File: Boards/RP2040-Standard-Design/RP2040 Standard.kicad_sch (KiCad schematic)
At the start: 38 parts, among them J2 BM03B-SRSS-TBLFSN, J4 DX07S016JA1R1500, U1 ST1L05APU33R, U2 W25Q128JVSIQ TR, U3 ESD7L5.0DT5G

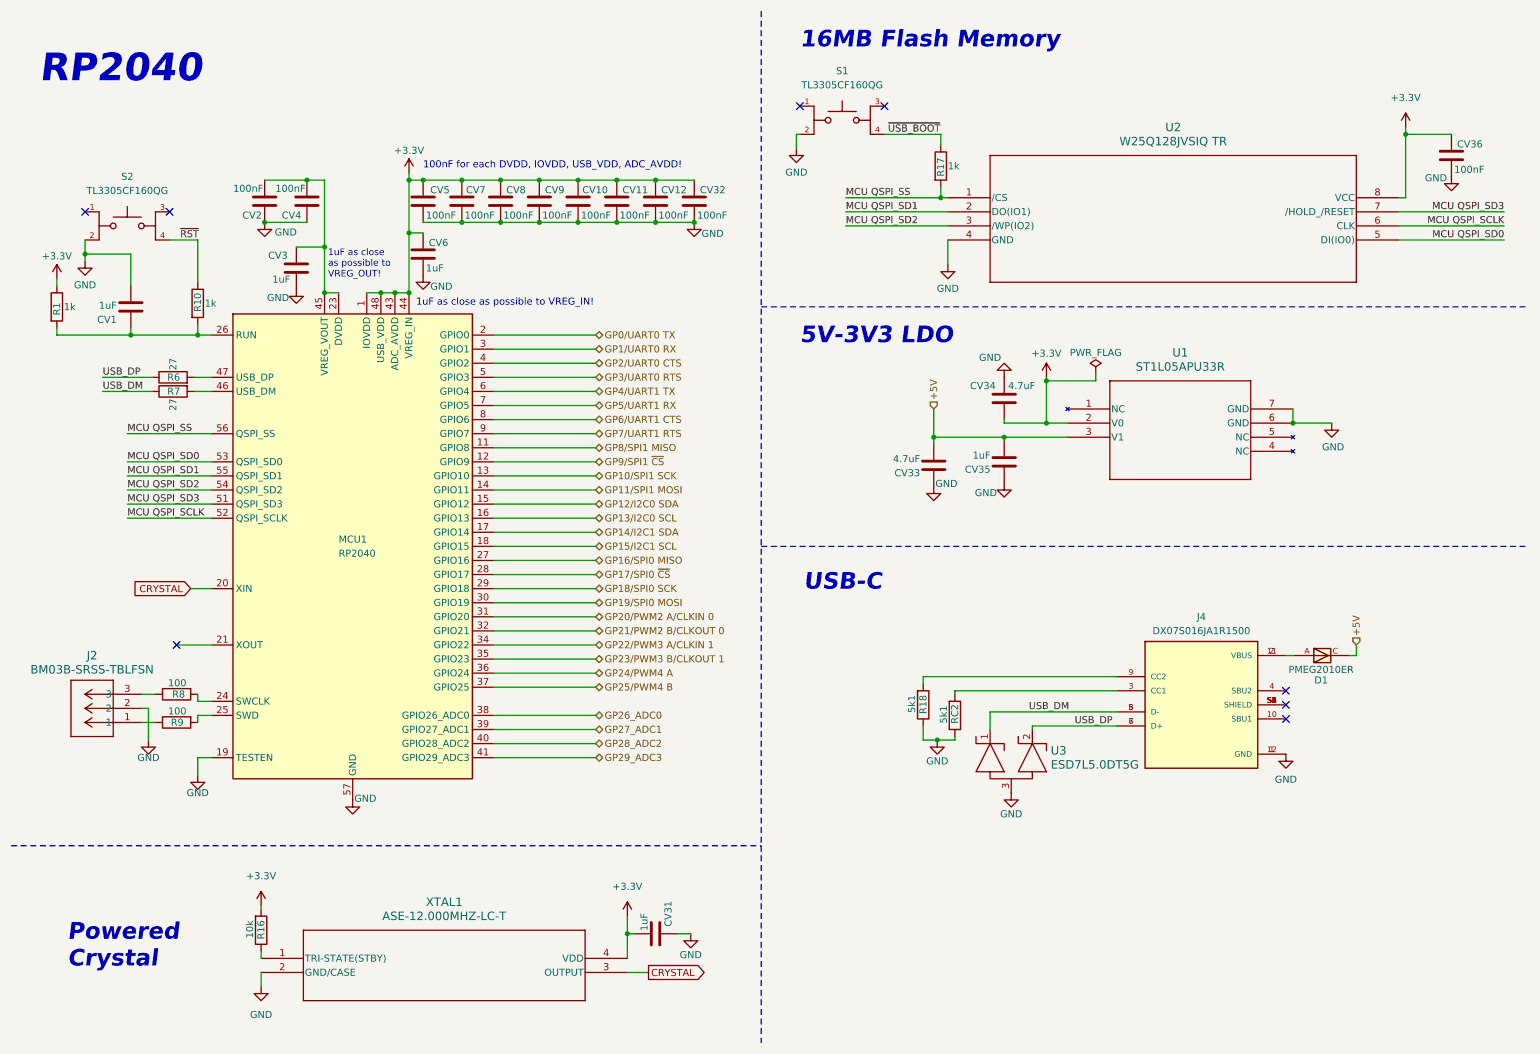
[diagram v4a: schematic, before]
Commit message: changes in RP2040 design
GPIO25 LED is now part of RP2040 Standard
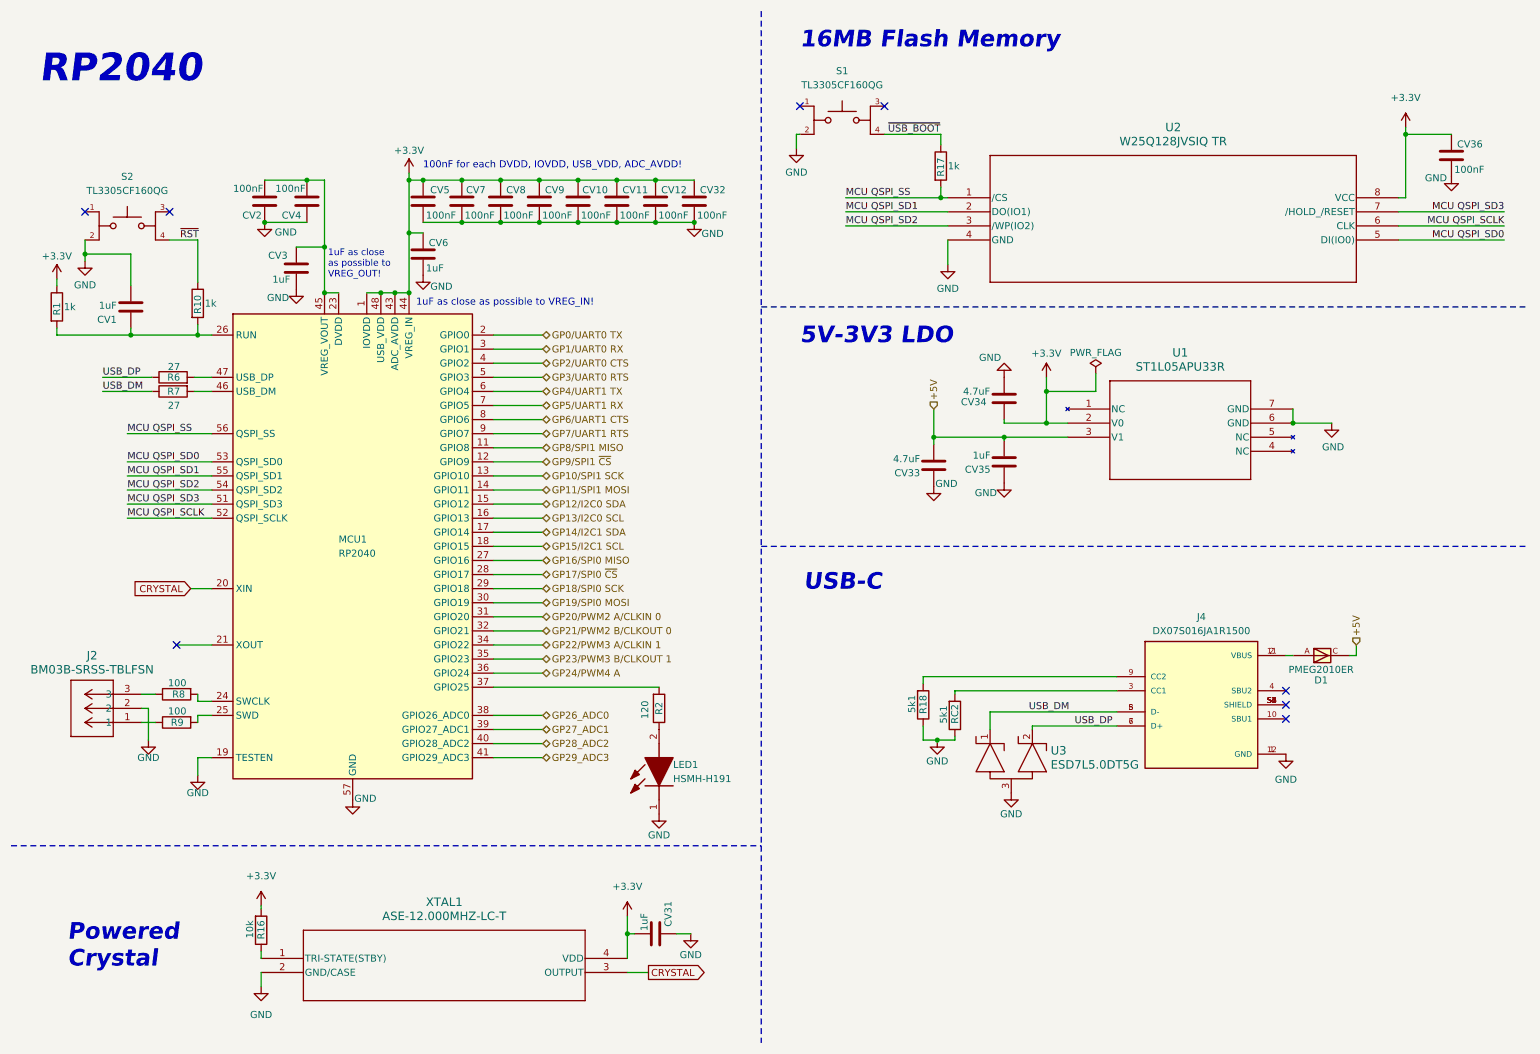
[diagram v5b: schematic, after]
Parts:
- added LED1: HSMH-H191, MAG LIS2MDLTR:LGA-12_2X2X1_STM, symbol Red SMD LED:HSMH-H191
- added R2: 120, RC0402N_VIS:RC0402N_VIS, symbol Device:R
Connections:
- net GND: now also LED1.1 (K)
- net GP25/PWM4 B: no longer names the net of MCU1.37 (GPIO25)
- net GP25/PWM4 B: now also R2.2
- new net: LED1.2 (A), R2.1

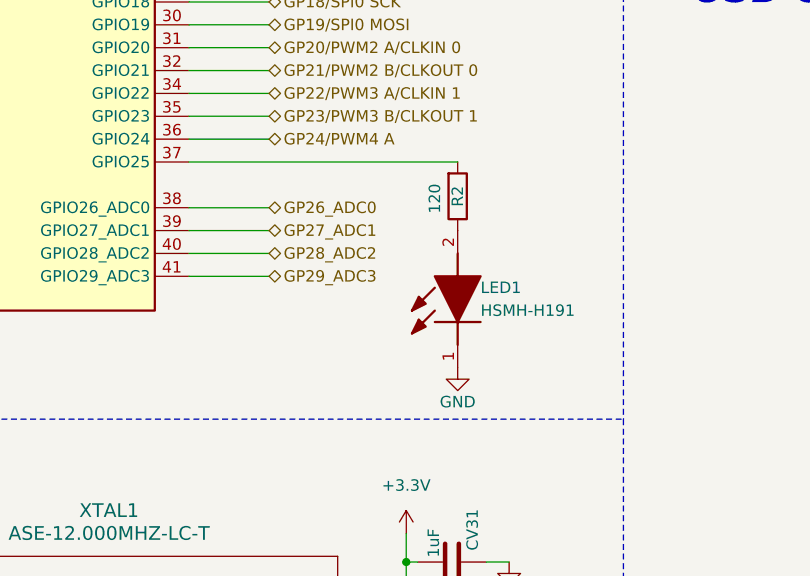
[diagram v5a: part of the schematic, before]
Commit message: Reorganização da biblioteca de simbolos por categorias
A SymbolsLib foi atualizada para estar por categorias
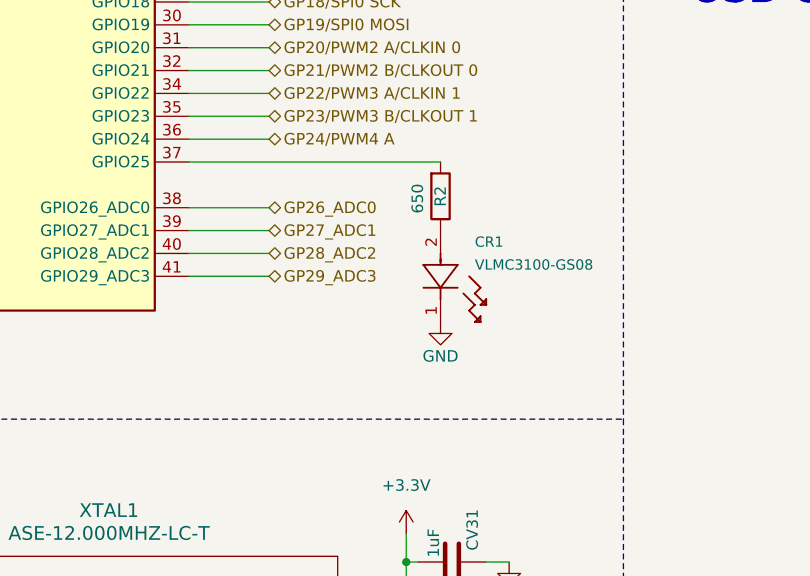
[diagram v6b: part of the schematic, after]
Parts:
- removed LED1: HSMH-H191, MAG LIS2MDLTR:LGA-12_2X2X1_STM, symbol Red SMD LED:HSMH-H191
- added CR1: VLMC3100-GS08, LED_PLCC_VSMB, symbol GreenLED__VLMC3100-GS08:VLMC3100-GS08
- R2: value 120 -> 650
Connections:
- net GND: now also CR1.1
- net at R2.1: now also CR1.2
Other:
- moved on the sheet: R2
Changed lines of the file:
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@@
 	(wire
 		(pts
-			(xy 99.06 133.985) (xy 128.905 133.985)
+			(xy 99.06 133.985) (xy 127 133.985)
 		)
 		(stroke
@@
 	(symbol
 		(lib_id "Device:R")
-		(at 128.905 137.795 0)
+		(at 127 137.795 0)
 		(mirror x)
 		(unit 1)
@@
 		(dnp no)
 		(property "Reference" "R2"
-			(at 128.905 137.795 90)
+			(at 127 137.795 90)
 			(effects
 				(font
@@
 			)
 		)
-		(property "Value" "120"
-			(at 126.365 138.049 90)
+		(property "Value" "650"
+			(at 124.46 138.049 90)
 			(effects
 				(font
@@
 		)
 		(property "Footprint" "RC0402N_VIS:RC0402N_VIS"
-			(at 127.127 137.795 90)
+			(at 125.222 137.795 90)
 			(effects
 				(font
@@
 		)
 		(property "Datasheet" "~"
-			(at 128.905 137.795 0)
+			(at 127 137.795 0)
 			(effects
 				(font
@@
 		)
 		(property "Description" "Resistor"
-			(at 128.905 137.795 0)
+			(at 127 137.795 0)
 			(effects
 				(font
@@
 	)
 	(symbol
+		(lib_id "GreenLED__VLMC3100-GS08:VLMC3100-GS08")
+		(at 127 141.605 270)
+		(unit 1)
+		(exclude_from_sim no)
+		(in_bom yes)
+		(on_board yes)
+		(dnp no)
+		(property "Reference" "CR1"
+			(at 130.81 142.875 90)
+			(effects
+				(font
+					(size 1.143 1.143)
+				)
+				(justify left)
+			)
+		)
+		(property "Value" "VLMC3100-GS08"
+			(at 130.81 145.415 90)
+			(effects
+				(font
+					(size 1.143 1.143)
+				)
+				(justify left)
+			)
+		)
+		(property "Footprint" "LED_PLCC_VSMB"
+			(at 127 141.605 0)
+			(effects
+				(font
+					(size 1.27 1.27)
+					(italic yes)
+				)
+				(hide yes)
+			)
+		)
+		(property "Datasheet" "VLMC3100-GS08"
+			(at 127 141.605 0)
+			(effects
+				(font
+					(size 1.27 1.27)
+					(italic yes)
+				)
+				(hide yes)
+			)
+		)
+		(property "Description" ""
+			(at 127 141.605 0)
+			(effects
+				(font
+					(size 1.27 1.27)
+				)
+				(hide yes)
+			)
+		)
+		(pin "1"
+		)
+		(pin "2"
+		)
+		(instances
+			(project ""
+				(path "/7712695e-3038-4da8-a54c-20dbd93db58d/3d4082b5-a5ce-4208-94d0-5d9dbdc70dd6"
+					(reference "CR1")
+					(unit 1)
+				)
+			)
+		)
+	)
+	(symbol
 		(lib_id "Device:R")
 		(at 57.15 177.8 0)
@@
 	(symbol
 		(lib_id "power:GND")
-		(at 128.905 156.845 0)
+		(at 127 151.765 0)
 		(unit 1)
 		(exclude_from_sim no)
@@
 		(dnp no)
 		(property "Reference" "#PWR04"
-			(at 128.905 163.195 0)
+			(at 127 158.115 0)
 			(effects
 				(font
@@
 		)
 		(property "Value" "GND"
-			(at 128.905 160.655 0)
+			(at 127 155.575 0)
 			(effects
 				(font
@@
 		)
 		(property "Footprint" ""
-			(at 128.905 156.845 0)
+			(at 127 151.765 0)
 			(effects
 				(font
@@
 		)
 		(property "Datasheet" ""
-			(at 128.905 156.845 0)
+			(at 127 151.765 0)
 			(effects
 				(font
@@
 		)
 		(property "Description" "Power symbol creates a global label with name \"GND\" , ground"
-			(at 128.905 156.845 0)
+			(at 127 151.765 0)
 			(effects
 				(font
@@
 					(unit 1)
 				)
-			)
-		)
-	)
-	(symbol
-		(lib_id "Red SMD LED:HSMH-H191")
-		(at 128.905 156.845 90)
-		(unit 1)
-		(exclude_from_sim no)
-		(in_bom yes)
-		(on_board yes)
-		(dnp no)
-		(property "Reference" "LED1"
-			(at 131.445 147.955 90)
-			(effects
-				(font
-					(size 1.27 1.27)
-				)
-				(justify right)
-			)
-		)
-		(property "Value" "HSMH-H191"
-			(at 131.445 150.495 90)
-			(effects
-				(font
-					(size 1.27 1.27)
-				)
-				(justify right)
-			)
-		)
-		(property "Footprint" "MAG LIS2MDLTR:LGA-12_2X2X1_STM"
-			(at 222.555 144.145 0)
-			(effects
-				(font
-					(size 1.27 1.27)
-				)
-				(justify left bottom)
-				(hide yes)
-			)
-		)
-		(property "Datasheet" "https://www.broadcom.com/products/leds-and-displays/chip-leds/0603-1.6-x-0.88mm-top-mount/hsmh-h191"
-			(at 322.555 144.145 0)
-			(effects
-				(font
-					(size 1.27 1.27)
-				)
-				(justify left bottom)
-				(hide yes)
-			)
-		)
-		(property "Description" "0603 Top Mount Mono-Color ChipLED"
-			(at 128.905 156.845 0)
-			(effects
-				(font
-					(size 1.27 1.27)
-				)
-				(hide yes)
-			)
-		)
-		(property "Height" "0.7"
-			(at 522.555 144.145 0)
-			(effects
-				(font
-					(size 1.27 1.27)
-				)
-				(justify left bottom)
-				(hide yes)
-			)
-		)
-		(property "Manufacturer_Name" "Avago Technologies"
-			(at 622.555 144.145 0)
-			(effects
-				(font
-					(size 1.27 1.27)
-				)
-				(justify left bottom)
-				(hide yes)
-			)
-		)
-		(property "Manufacturer_Part_Number" "HSMH-H191"
-			(at 722.555 144.145 0)
-			(effects
-				(font
-					(size 1.27 1.27)
-				)
-				(justify left bottom)
-				(hide yes)
-			)
-		)
-		(property "Mouser Part Number" "630-HSMH-H191"
-			(at 822.555 144.145 0)
-			(effects
-				(font
-					(size 1.27 1.27)
-				)
-				(justify left bottom)
-				(hide yes)
-			)
-		)
-		(property "Mouser Price/Stock" "https://www.mouser.co.uk/ProductDetail/Broadcom-Avago/HSMH-H191?qs=Li%252BoUPsLEnsN8XNfO1JPnw%3D%3D"
-			(at 922.555 144.145 0)
-			(effects
-				(font
-					(size 1.27 1.27)
-				)
-				(justify left bottom)
-				(hide yes)
-			)
-		)
-		(property "Arrow Part Number" ""
-			(at 1022.555 144.145 0)
-			(effects
-				(font
-					(size 1.27 1.27)
-				)
-				(justify left bottom)
-				(hide yes)
-			)
-		)
-		(property "Arrow Price/Stock" ""
-			(at 1122.555 144.145 0)
-			(effects
-				(font
-					(size 1.27 1.27)
-				)
-				(justify left bottom)
-				(hide yes)
-			)
-		)
-		(pin "2"
-		)
-		(pin "1"
-		)
-		(instances
-			(project "RP2040 Standard Design"
-				(path "/7712695e-3038-4da8-a54c-20dbd93db58d/3d4082b5-a5ce-4208-94d0-5d9dbdc70dd6"
-					(reference "LED1")
-					(unit 1)
-				)
